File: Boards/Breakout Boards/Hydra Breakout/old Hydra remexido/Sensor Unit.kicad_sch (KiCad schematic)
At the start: 79 parts, among them IC5 INA2181A4IDSQR, IC6 PCA9306GM,125, IC7 INA181A4QDCKRQ1, U1 MAX31856MUD+T, U10 STLM20DD9F, U11 MAX31856MUD+T, U15 AD8040ARUZ, U16 AD8040ARUZ, U3 MAX31856MUD+T, U8 max11614eee+

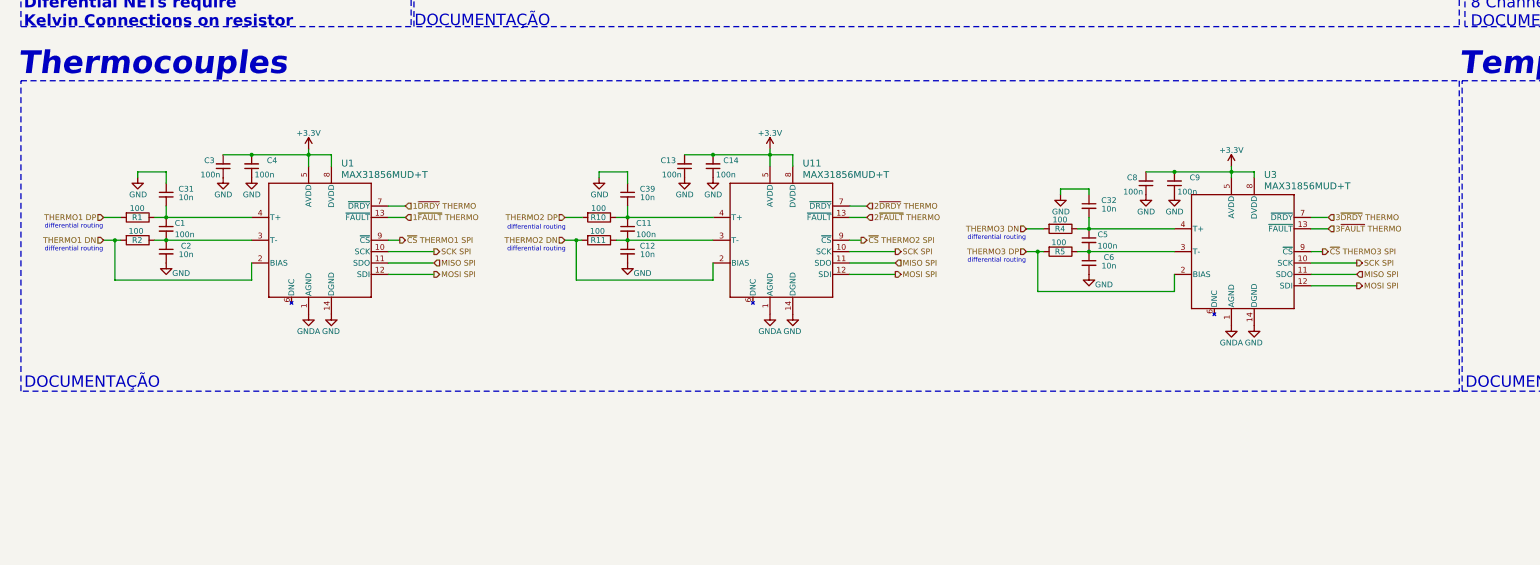
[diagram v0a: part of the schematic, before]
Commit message: Design da Hydra Breakout (Part 1)
Inclui algumas adições à biblioteca.
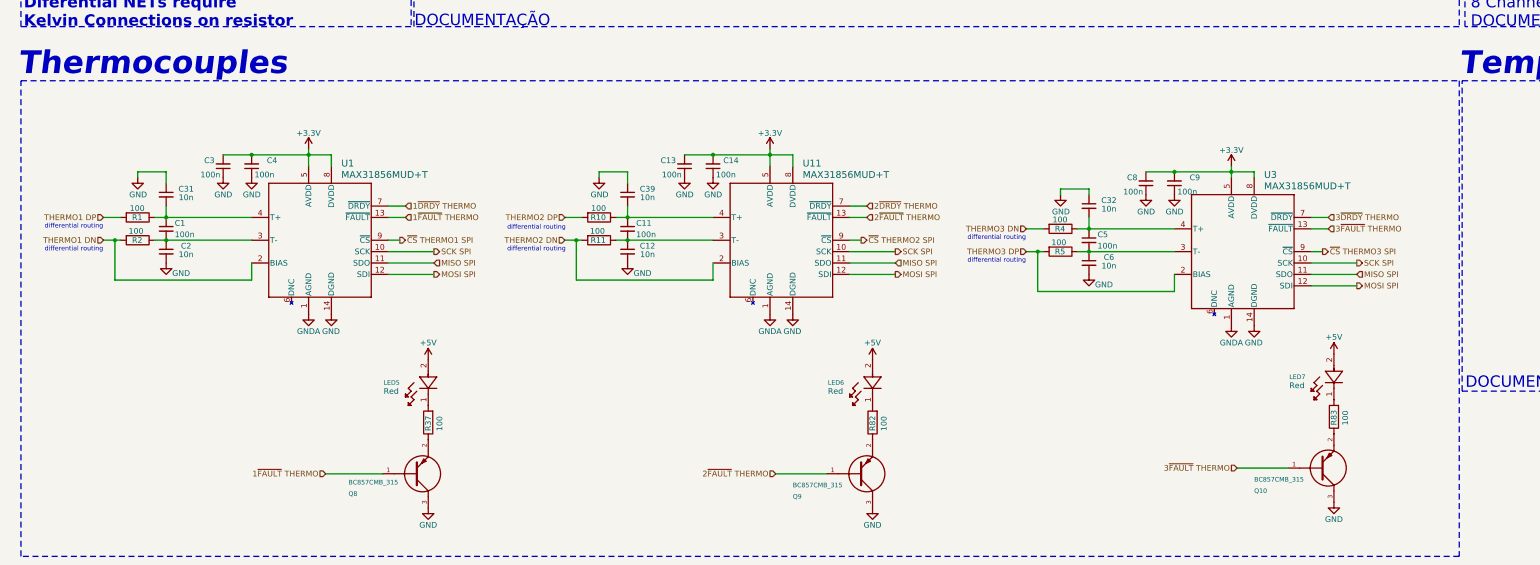
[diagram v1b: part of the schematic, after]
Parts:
- added LED5, LED6, LED7: VLMS1500-GS08, LED-Red_VLMS1500-GS08:LED_00-GS08_VIS_RED, symbol VLMS1500-GS08:VLMS1500-GS08
- added Q10, Q8, Q9: BC857CMB_315, PNP_BC857CMB_315:TRANS_PMZB550UNEYL, symbol BC857CMB_315:BC857CMB_315
- added R37, R82, R83: 100, Resistor-0402:RES_0402, symbol Device:R
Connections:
- net +5V: now also LED5.2, LED6.2, LED7.2
- net 1~{FAULT} THERMO: now also Q8.1
- net 2~{FAULT} THERMO: now also Q9.1
- net 3~{FAULT} THERMO: now also Q10.1
- net GND: now also Q10.3, Q8.3, Q9.3
- new net: Q9.2, R82.1
- new net: Q10.2, R83.1
- new net: LED7.1, R83.2
- new net: LED6.1, R82.2
- new net: Q8.2, R37.1
- new net: LED5.1, R37.2
